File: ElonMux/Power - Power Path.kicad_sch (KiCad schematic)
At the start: 72 parts, among them IC801 LTC7000EMSE#PBF, IC802 LTC7000EMSE#PBF, IC803 TPS3701DDCR, Q801 CSD18540Q5B, Q802 CSD18540Q5B, Q803 CSD18540Q5B, Q804 CSD18540Q5B

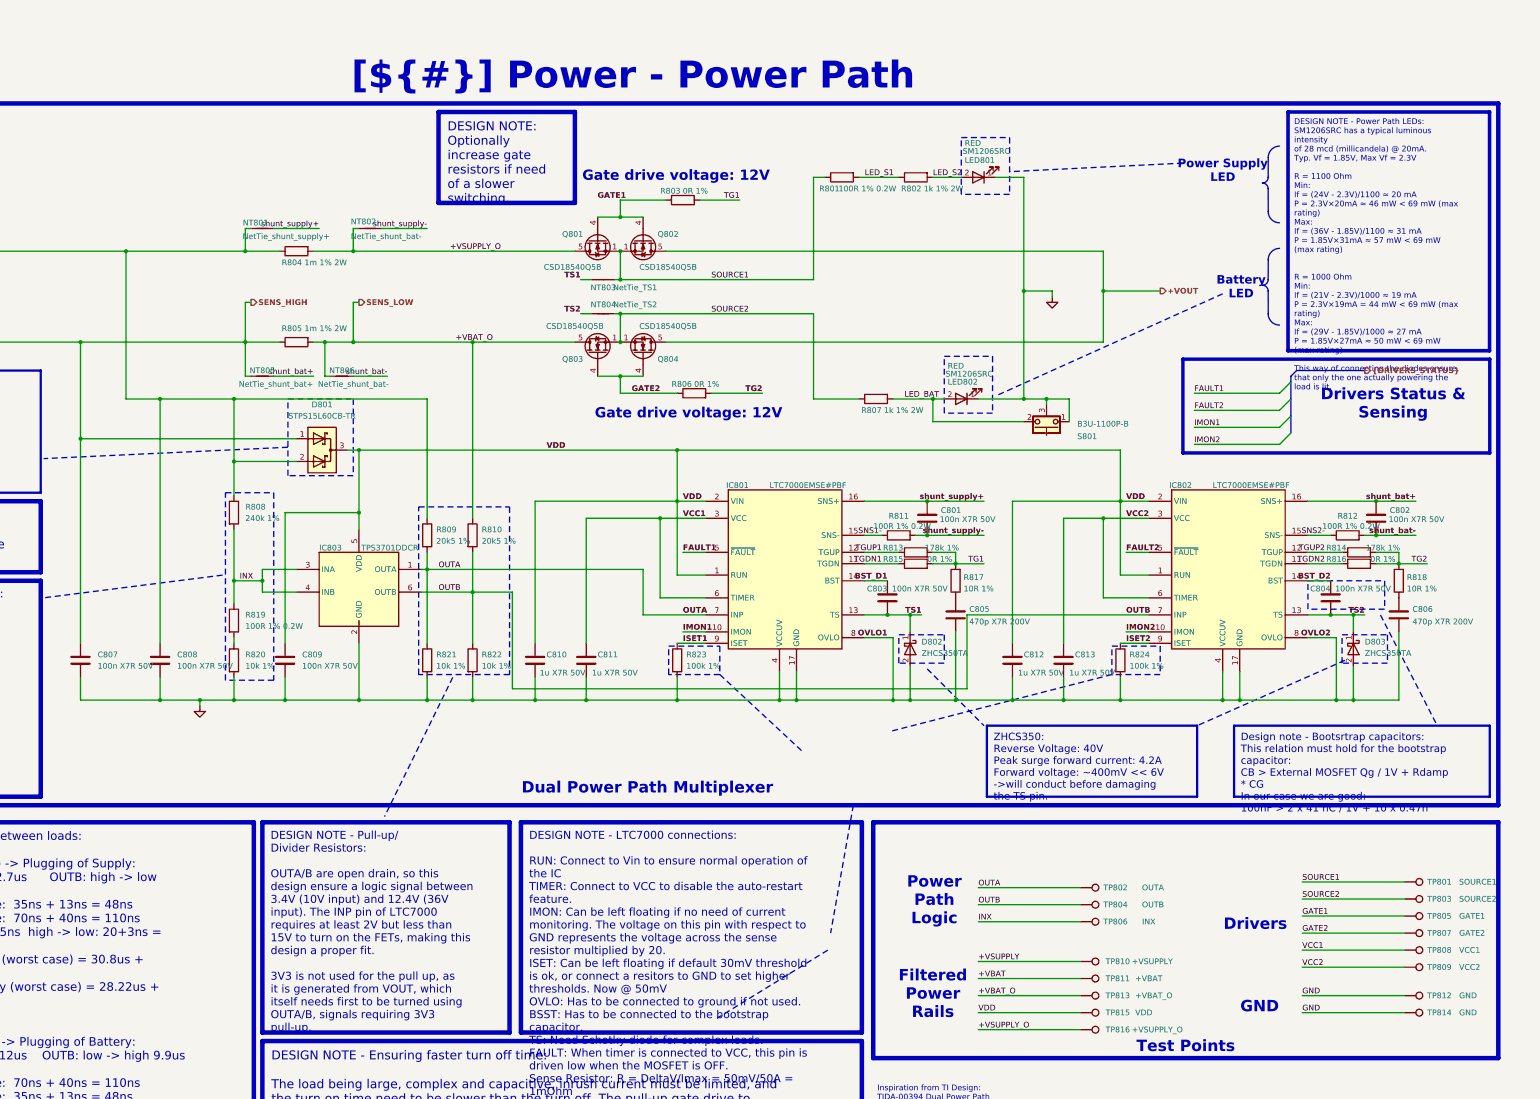
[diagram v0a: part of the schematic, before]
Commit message: Done with changes of v1.1, need to final check and order
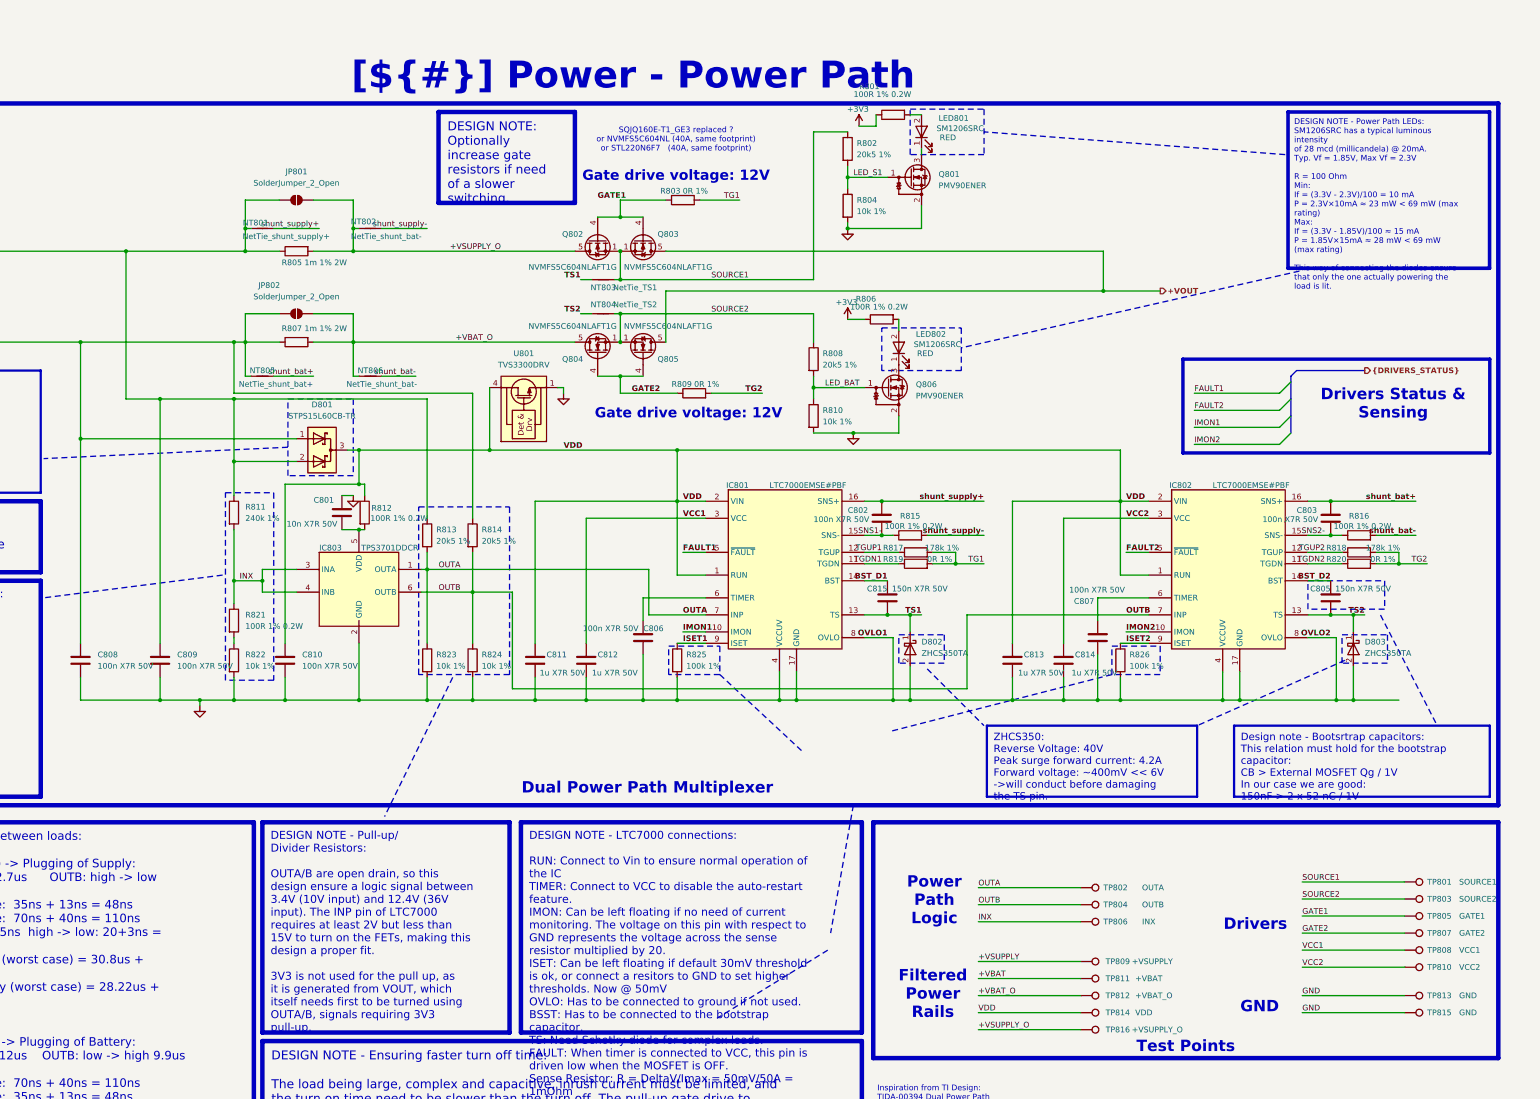
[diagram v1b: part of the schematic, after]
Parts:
- removed C803: 100n X7R 50V, Capacitor_SMD:C_0402_1005Metric, symbol Device:C
- removed C805: 470p X7R 200V, Capacitor_SMD:C_0603_1608Metric_Pad1.08x0.95mm_HandSolder, symbol Device:C
- removed Q802: CSD18540Q5B, Package_TO_SOT_SMD:TDSON-8-1, symbol Transistor_FET:CSD18540Q5B
- removed R807: 1k 1% 2W, Resistor_SMD:R_2010_5025Metric, symbol Device:R
- removed R817, R818: 10R 1%, Resistor_SMD:R_0402_1005Metric, symbol Device:R
- removed S801: B3U-1100P-B, Charge_Manager_FP:B3U1100PB, symbol Charge_Manager_SYM:B3U-1100P
- added C801: 10n X7R 50V, Capacitor_SMD:C_0402_1005Metric, symbol Device:C
- added C807: 100n X7R 50V, Capacitor_SMD:C_0402_1005Metric, symbol Device:C
- added C815: 150n X7R 50V, Capacitor_SMD:C_0603_1608Metric, symbol Device:C
- added JP801, JP802: SolderJumper_2_Open, Jumper:SolderJumper-2_P1.3mm_Open_RoundedPad1.0x1.5mm, symbol Jumper:SolderJumper_2_Open
- added Q801, Q806: PMV90ENER, Package_TO_SOT_SMD:SOT-23-3, symbol 0_transistor_fet:PMV90ENER
- added Q805: NVMFS5C604NLAFT1G, Charge_Manager_FP:ONSemi_SO-8FL-4, symbol Transistor_FET:CSD18540Q5B
- added R804, R810: 10k 1%, Resistor_SMD:R_0402_1005Metric, symbol Device:R
- added R806, R812: 100R 1% 0.2W, Resistor_SMD:R_0402_1005Metric, symbol Device:R
- added R808: 20k5 1%, Resistor_SMD:R_0402_1005Metric, symbol Device:R
- added U801: TVS3300DRV, Package_SON:WSON-6-1EP_2x2mm_P0.65mm_EP1x1.6mm, symbol Power_Protection:TVS3300DRV
- C805: renamed from C804; value 100n X7R 50V -> 150n X7R 50V; footprint Capacitor_SMD:C_0402_1005Metric -> Capacitor_SMD:C_0603_1608Metric; Manufacturer TAIYO YUDEN -> KEMET; Manufacturer Part Number UMK105B7104KVHF -> C0603C154K5RACAUTO; Supplier Part Number 963-UMK105B7104KVHF -> 80-C0603C154K5RAUTO
- C806: value 470p X7R 200V -> 100n X7R 50V; footprint Capacitor_SMD:C_0603_1608Metric_Pad1.08x0.95mm_HandSolder -> Capacitor_SMD:C_0402_1005Metric; Manufacturer KYOCERA AVX -> TAIYO YUDEN; Manufacturer Part Number 06032C471KAT2A -> UMK105B7104KVHF; Supplier Part Number 581-06032C471KAT2A -> 963-UMK105B7104KVHF
- Q802: renamed from Q801; value CSD18540Q5B -> NVMFS5C604NLAFT1G; footprint Package_TO_SOT_SMD:TDSON-8-1 -> Charge_Manager_FP:ONSemi_SO-8FL-4; Manufacturer Texas Instruments -> onsemi; Manufacturer Part Number CSD18540Q5B -> NVMFS5C604NLAFT1G; Supplier Part Number 595-CSD18540Q5B -> 863-NVMFS5C604NLFT1G
- Q803, Q804: value CSD18540Q5B -> NVMFS5C604NLAFT1G; footprint Package_TO_SOT_SMD:TDSON-8-1 -> Charge_Manager_FP:ONSemi_SO-8FL-4; Manufacturer Texas Instruments -> onsemi; Manufacturer Part Number CSD18540Q5B -> NVMFS5C604NLAFT1G; Supplier Part Number 595-CSD18540Q5B -> 863-NVMFS5C604NLFT1G
- R802: value 1k 1% 2W -> 20k5 1%; footprint Resistor_SMD:R_2010_5025Metric -> Resistor_SMD:R_0402_1005Metric; Manufacturer TE Connectivity / Holsworthy -> KOA Speer; Manufacturer Part Number 35021K0FT -> RK73H1ETTP2052F; Supplier Part Number 279-35021K0FT -> 660-RK73H1ETTP2052F
- renumbered C801 to C802, C802 to C803, C807 to C808, C808 to C809, C809 to C810, C810 to C811, C811 to C812, C812 to C813, C813 to C814, R804 to R805, R805 to R807, R806 to R809, R808 to R811, R809 to R813, R810 to R814, R811 to R815, R812 to R816, R813 to R817, R814 to R818, R815 to R819, R816 to R820, R819 to R821, R820 to R822, R821 to R823, R822 to R824, R823 to R825, R824 to R826, TP810 to TP809, TP809 to TP810, TP813 to TP812, TP812 to TP813, TP815 to TP814, TP814 to TP815
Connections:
- net +VBAT: now also R814.1, JP802.1 (A)
- net +VOUT: now also Q803.5 (D), Q805.5 (D); no longer Q804.5 (D)
- net +VSUPPLY: now also JP801.1 (A)
- net +VSUPPLY_O: now also JP801.2 (B)
- net BST_D1: now also C815.1
- net GATE1: now also Q803.4 (G)
- net GATE2: now also Q805.4 (G); no longer Q803.4 (G)
- net GND: now also C801.1, C807.2, Q801.2 (S), Q806.2 (S), R804.2, R810.2, U801.1 (GND), U801.2 (GND), U801.3 (GND), U801.7 (GND); no longer LED801.1 (K), LED802.1 (K)
- net LED_BAT: now also Q806.1 (G), R808.2, R810.1; no longer LED802.2 (A)
- net LED_S1: now also R802.2, Q801.1 (G), R804.1; no longer R801.2, R802.1
- net SNS1-: now also C802.1
- net SNS2-: now also C803.1
- net SOURCE1: now also Q803.1 (S), Q803.2 (S), Q803.3 (S), R802.1; no longer R801.1
- net SOURCE2: now also Q805.1 (S), Q805.2 (S), Q805.3 (S), R808.1; no longer Q803.1 (S), Q803.2 (S), Q803.3 (S)
- net TS1: now also C815.2
- net VCC1: no longer IC801.6 (TIMER)
- net VCC2: no longer IC802.6 (TIMER)
- net VDD: now also R812.1, U801.4 (IN), U801.5 (IN), U801.6 (IN); no longer IC803.5 (VDD)
- net shunt_bat-: no longer C803.1
- net shunt_supply-: no longer C802.1
- net at C806.1: now also IC801.6 (TIMER)
- net LED_S2: no longer names the net of LED801.2 (A)
- net LED_S2: now also R801.2; no longer R802.2
- net SENS_LOW renamed +VBAT_O
- net +VBAT_O: now also Q804.5 (D), JP802.2 (B); no longer Q803.5 (D), R814.1
- new net: LED801.1 (K), Q801.3 (D)
- new net: C801.2, IC803.5 (VDD), R812.2
- new net: LED802.2 (A), R806.2
- new net: C807.1, IC802.6 (TIMER)
- new net: LED802.1 (K), Q806.3 (D)
- new net +3V3: R801.1, R806.1
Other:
- note added: "SQJQ160E-T1_GE3 replaced ? or NVMFS5C604NL (40A, same footprint) or STL220N6F7 (40A, same footprint)"
- moved on the sheet: C802, C803, NT806, R815, R816

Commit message: Finished V1.1, maybe extra cleaning needed of some details in the doc
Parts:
- TP809, TP812: footprint Charge_Manager_FP:TestPoint_Pad_D0.5mm_Front -> TestPoint:TestPoint_THTPad_D2.5mm_Drill1.2mm
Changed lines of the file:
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@@
 	(title_block
 		(title "Power - Power Path")
-		(date "2025-06-17")
+		(date "2025-07-24")
 		(rev "${REVISION}")
 		(company "${COMPANY}")
@@
 			"YQAAADMAAABKAAAANwAAAHYAAABKAAAAMwAAAHgAAABaAAAAQwAAAG0AAABkAAAAZAAAADcAAABo"
 			"AAAAYgAAACsAAAA2AAAAMwAAAE8AAABEAAAAagAAADUAAAAyAAAAZAAAADUAAABmAAAATgAAADAA"
-			"AAA1AAAATQAAAA=="
+			"AAA1AAAATQAAAAAAAAAAAAAAAAAAAAAAAAAAAAAAAAAAAAAAAAAAAAAAAAAAAAAAAAAAAAAAAAAA"
+			"AAAAAAAAAAAAAAAAAAAAAAAAAAAAAAAAAAAAAAAAAAAAAAAAAAAAAAAAAAAAAAAAAAAAAAAAAAAA"
+			"AAAAAAAAAAAAAAAAAAAAAAAAAAAAAAAAAAAAAAAAAAAAAAAAAAAAAAAAAAAAAAAAAAAAAAAAAAAA"
+			"AAAAAAAAAAAAAAAAAAAAAAAAAAAAAAAAAAAAAAAAAAAAAAAAAAAAAAAAAAAAAAAAAAAAAAAAAAAA"
+			"AAAAAAAAAAAAAAAAAAAAAAAAAAAAAAAAAAAAAAAAAAAAAAAAAAAAAAAAAAAAAAAAAAAAAAAAAAAA"
+			"AAAAAAAAAAAAAAAAAAAAAAAAAAAAAAAAAAAAAAAAAAAAAAAAAAAAAAAAAAAAAAAAAAAAAAAAAAAA"
+			"AAAAAAAAAAAAAAAAAAAAAAAAAAAAAAAAAAAAAAAAAAAAAAAAAAAAAAAAAAAAAAAAAAAAAAAAAAAA"
+			"AAAAAAAAAAAAAAAAAAAAAAAAAAAAAAAAAAAAAAAAAAAAAAAAAAAAAAAAAAAAAAAAAAAAAAAAAAAA"
+			"AAAAAAAAAAAAAAAAAAAAAAAAAAAAAAAAAAAAAAAAAAAAAAAAAAAAAAAAAAAAAAAAAAAAAAAAAAAA"
+			"AAAAAAAAAAAAAAAAAAAAAAAAAAAAAAAAAAAAAAAAAAAAAAAAAAAAAAAAAAAAAAAAAAAAAAAAAAAA"
+			"AAAAAAAAAAAAAAAAAAAAAAAAAAAAAAAAAAAAAAAAAAAAAAAAAAAAAAAAAAAAAAAAAAAAAAAAAAAA"
+			"AAAAAAAAAAAAAAAAAAAAAAAAAAAAAAAAAAAAAAAAAAAAAAAAAAAAAAAAAAAAAAAAAAAAAAAAAAAA"
+			"AAAAAAAAAAAAAAAAAAAAAAAAAAAAAAAAAAAAAAAAAAAAAAAAAAAAAAAAAAAAAAAAAAAAAAAAAAAA"
+			"AAAAAAAAAAAAAAAAAAAAAAAAAAAAAAAAAAAAAAAAAAAAAAAAAAAAAAAAAAAAAAAAAAAAAAAAAAAA"
+			"AAAAAAAAAAAAAAAAAAAAAAAAAAAAAAAAAAAAAAAAAAAAAAAAAAAAAAAAAAAAAAAAAAAAAAAAAAAA"
+			"AAAAAAAAAAAAAAAAAAAAAAAAAAAAAAAAAAAAAAAAAAAAAAAAAAAAAAAAAAAAAAAAAAAAAAAAAAAA"
+			"AAAAAAAAAAAAAAAAAAAAAAAAAAAAAAAAAAAAAAAAAAAAAAAAAAAAAAAAAAAAAAAAAAAAAAAAAAAA"
+			"AAAAAAAAAAAAAAAAAAAAAAAAAAAAAAAAAAAAAAAAAAAAAAAAAAAAAAAAAAAAAAAAAAAAAAAAAAAA"
+			"AAAAAAAAAAAAAA=="
 		)
 	)
@@
 			)
 		)
-		(property "Footprint" "Charge_Manager_FP:TestPoint_Pad_D0.5mm_Front"
+		(property "Footprint" "TestPoint:TestPoint_THTPad_D2.5mm_Drill1.2mm"
 			(at 309.88 214.63 0)
 			(effects
@@
 			)
 		)
-		(property "Footprint" "Charge_Manager_FP:TestPoint_Pad_D0.5mm_Front"
+		(property "Footprint" "TestPoint:TestPoint_THTPad_D2.5mm_Drill1.2mm"
 			(at 309.88 222.25 0)
 			(effects

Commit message: Small adjustments
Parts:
- U801: Manufacturer (none) -> Texas Instruments; Manufacturer Part Number (none) -> TVS3300DRVR; Supplier (none) -> Mouser Electronics; Supplier Part Number (none) -> 595-TVS3300DRVR
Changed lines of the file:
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@@
 			"AAAAAAAAAAAAAAAAAAAAAAAAAAAAAAAAAAAAAAAAAAAAAAAAAAAAAAAAAAAAAAAAAAAAAAAAAAAA"
 			"AAAAAAAAAAAAAAAAAAAAAAAAAAAAAAAAAAAAAAAAAAAAAAAAAAAAAAAAAAAAAAAAAAAAAAAAAAAA"
-			"AAAAAAAAAAAAAA=="
+			"AAAAAAAAAAAAAAAAVgAAAHYAAAA3AAAASAAAAGIAAABEAAAAVgAAAC8AAABJAAAAWAAAAG0AAABS"
+			"AAAAaQAAAHQAAABnAAAAegAAAEMAAABXAAAAVAAAAFIAAAA5AAAAUgAAAHAAAABvAAAASwAAAC8A"
+			"AAA5AAAAagAAAHQAAABwAAAAcQAAAC8AAABrAAAATAAAAHgAAABJAAAAUgAAAGUAAAB5AAAAWgAA"
+			"AEIAAABMAAAATAAAAG8AAABxAAAAUAAAAG0AAAByAAAAMwAAADkAAABzAAAAMwAAAFgAAABmAAAA"
+			"TAAAADgAAABwAAAAMAAAADcAAAAvAAAAKwAAAHUAAAByAAAATAAAAGUAAAB0AAAATAAAADcAAABa"
+			"AAAAMAAAADQAAABxAAAAMQAAAE0AAAArAAAAaQAAADUAAABNAAAATwAAAGwAAABEAAAAcQAAAGMA"
+			"AABQAAAAMwAAAHYAAABZAAAATwAAADAAAAAwAAAAawAAAEgAAAAzAAAAbwAAAE0AAABHAAAAbQAA"
+			"ADQAAAAzAAAAdAAAAFIAAABaAAAAeAAAAEUAAABRAAAAYgAAAGwAAABlAAAANAAAADcAAABWAAAA"
+			"TQAAADUAAAArAAAAcQAAAEcAAAAzAAAASwAAAFUAAAB3AAAAVQAAAGgAAABGAAAAVAAAAFEAAABH"
+			"AAAARAAAAFIAAAA5AAAAUgAAAHEAAABLAAAAMgAAAHoAAABuAAAAWAAAADUAAAB6AAAAKwAAAGUA"
+			"AAByAAAAWQAAAGIAAABjAAAAWgAAAGEAAABJAAAAaQAAAEYAAABUAAAARQAAAEYAAABCAAAAQgAA"
+			"AFoAAABkAAAAcgAAADYAAABIAAAANAAAAHEAAAA4AAAAcgAAAC8AAABKAAAAegAAADcAAAB4AAAA"
+			"aQAAAGUAAABtAAAAMAAAADAAAAAwAAAANgAAAGYAAAAzAAAAdgAAAHMAAABIAAAANwAAADIAAABs"
+			"AAAAegAAAFcAAABqAAAAOAAAAHkAAAAxAAAAWAAAADcAAABUAAAAcwAAAFUAAABpAAAAYQAAADQA"
+			"AAByAAAAegAAAHoAAAB6AAAAcAAAAHQAAABPAAAAUAAAACsAAABPAAAATQAAADkAAABHAAAAbAAA"
+			"AHAAAABlAAAAOQAAADAAAABMAAAATAAAAHoAAAA1AAAAUwAAAEUAAABhAAAAZQAAACsAAABtAAAA"
+			"bQAAAFAAAABSAAAAOQAAAFIAAABxAAAAdgAAAE4AAABhAAAAcQAAAGIAAAB2AAAAMQAAAEEAAAA1"
+			"AAAAVQAAAGgAAABGAAAANwAAAFMAAAAwAAAAQQAAAFcAAABYAAAAYQAAACsAAABCAAAAdAAAAG0A"
+			"AAA4AAAARgAAAL0B0C1iAAAAAAAAgU6CzAGBiKAtYgAAAAAAAILeAYL9AREAggUC4IIMAuCCFALg"
+			"ghwC4ND+YgAAAAAAAIFOgaiByBECgc7QrmIAAAAAAACBToHcgfiCh1aCSAEUAAAAIIJRAdCuYgAA"
+			"AAAAAIFOgX+BiKCuYgAAAAAAAPgAAAAAAAAAAPgNAAAAAAAAAPgTAAAAAAAAAPiGAAAAAAAAAIKK"
+			"AeCCjgHggpYB4IKeAeCCpQHggq4B4IK2AeCCvQHQ6WIAAAAAAACBToLMAYGIoOliAAAAAAAAgt4B"
+			"gv0BEQCCBQLgggwC4IIUAuCCHALg0MNjAAAAAAAAgU6BqIHIEQKBztBzYwAAAAAAAIFOgdyB+IKH"
+			"VoJIARQAAAAgglEB0HNjAAAAAAAAgU6Bf4GIoHNjAAAAAAAA+AAAAAAAAAAA+A0AAAAAAAAA+BMA"
+			"AAAAAAAA+IYAAAAAAAAA+IMAAAAAAAAAgooB4IKOAeCClgHggp4B4IKlAeCCrgHggrYB4IK9AdCu"
+			"YwAAAAAAAIFOgswBgYigrmMAAAAAAACC3gGC/QERAIIFAuCCDALgghQC4IIcAuDQf2QAAAAAAACB"
+			"ToGogcgRAoHO0C9kAAAAAAAAgU6B3IH4godWgkgBFAAAACCCUQHQL2QAAAAAAACBToF/gYigL2QA"
+			"AAAAAAD4AAAAAAAAAAD4EwAAAAAAAAD4hgAAAAAAAAD4gwAAAAAAAACCigHggo4B4IKWAeCCngHg"
+			"gqUB4IKuAeCCtgHggr0B0GpkAAAAAAAAgU6CzAGBiKBqZAAAAAAAAILeAYL9AREAggUC4IIMAuCC"
+			"FALgghwC4NBbZQAAAAAAAIFOgaiByBECgc7QC2UAAAAAAACBToHcgfiCh1aCSAESAICC1wPQC2UA"
+			"AAAAAACBToJzFYKQFSIAAKBBgpkVIjMzMz+CohUiAACQQYKsFbCCshUiMzNzP4K8FcCCwhUiAABA"
+			"QYLLFSJmZuY+gtQVIgAAAEGC3hWwguQVIpqZWT+C7hXAgooB4IKOAeCClgHggp4B4IKlAeCCrgHg"
+			"grYB4IK9AdBGZQAAAAAAAIFOgswBgYigRmUAAAAAAACC3gGC/QERAIIFAuCCDALgghQC4IIcAuDQ"
+			"IGYAAAAAAACBToGogcgRAoHO0NBlAAAAAAAAgU6B3IH4godWgkgBFAAAACCCUQHQ0GUAAAAAAACB"
+			"ToF/gYig0GUAAAAAAAD4AAAAAAAAAAD4DQAAAAAAAAD4EwAAAAAAAAD4hgAAAAAAAAD4gwAAAAAA"
+			"AACCigHggo4B4IKWAeCCngHggqUB4IKuAeCCtgHggr0B0AtmAAAAAAAAgU6CzAGBiKALZgAAAAAA"
+			"AILeAYL9AREAgg=="
 		)
 	)
@@
 			(at 185.42 91.44 0)
 			(effects
+				(font
+					(size 1.27 1.27)
+				)
+				(hide yes)
+			)
+		)
+		(property "Manufacturer" "Texas Instruments"
+			(at 185.42 91.44 0)
+			(effects
+				(font
+					(size 1.27 1.27)
+				)
+				(hide yes)
+			)
+		)
+		(property "Manufacturer Part Number" "TVS3300DRVR"
+			(at 185.42 91.44 0)
+			(effects
+				(font
+					(size 1.27 1.27)
+				)
+				(hide yes)
+			)
+		)
+		(property "Supplier" "Mouser Electronics"
+			(at 185.42 91.44 0)
+			(effects
+				(font
+					(size 1.27 1.27)
+				)
+				(hide yes)
+			)
+		)
+		(property "Supplier Part Number" "595-TVS3300DRVR"
+			(at 185.42 91.44 0)
+			(effects
